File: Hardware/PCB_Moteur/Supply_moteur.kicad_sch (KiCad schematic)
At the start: 32 parts, among them J1 XT30PW-F, J19 XT30PW-F, U2 L6981N33DR

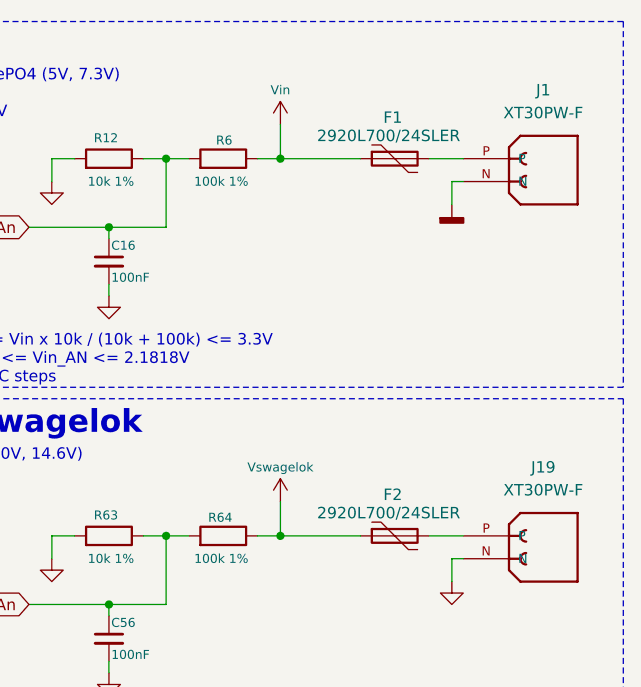
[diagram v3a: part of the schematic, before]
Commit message: fix : add polyfuses and fix 90 deg servo connectors
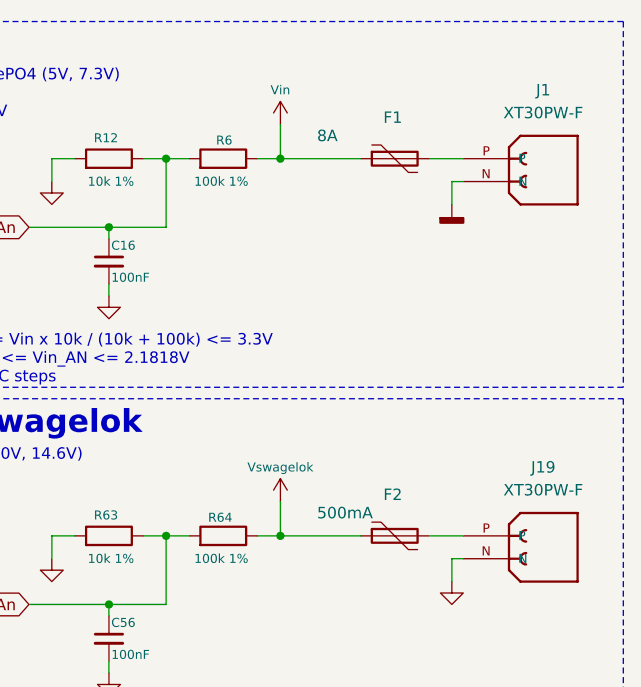
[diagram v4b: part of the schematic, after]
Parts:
- F1: value 2920L700/24SLER -> 8A; DigiKey_Part_Number (none) -> F8136CT-ND; Manufacturer_Part_Number (none) -> 2920L400/15MR
- F2: value 2920L700/24SLER -> 500mA; footprint Fuse:Fuse_2920_7451Metric -> Fuse:Fuse_0805_2012Metric; DigiKey_Part_Number (none) -> 18-0805L020/24YRCT-ND; Manufacturer_Part_Number (none) -> 0805L020/24YR
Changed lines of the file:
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@@
 			)
 		)
-		(property "Value" "2920L700/24SLER"
+		(property "Value" "8A"
 			(at 250.444 25.4 90)
 			(effects
@@
 			)
 		)
-		(property "Datasheet" ""
+		(property "Datasheet" "https://www.digikey.ca/en/products/detail/littelfuse-inc/2920L400-15MR/6234817"
 			(at 259.08 27.94 0)
 			(effects
@@
 		(property "Description" "Resettable fuse"
 			(at 259.08 27.94 0)
+			(effects
+				(font
+					(size 1.27 1.27)
+				)
+				(hide yes)
+			)
+		)
+		(property "DigiKey_Part_Number" "F8136CT-ND"
+			(at 259.08 27.94 90)
+			(effects
+				(font
+					(size 1.27 1.27)
+				)
+				(hide yes)
+			)
+		)
+		(property "Manufacturer_Part_Number" "2920L400/15MR"
+			(at 259.08 27.94 90)
 			(effects
 				(font
@@
 			)
 		)
-		(property "Value" "2920L700/24SLER"
+		(property "Value" "500mA"
 			(at 250.444 67.31 90)
 			(effects
@@
 			)
 		)
-		(property "Footprint" "Fuse:Fuse_2920_7451Metric"
+		(property "Footprint" "Fuse:Fuse_0805_2012Metric"
 			(at 264.16 71.12 0)
 			(effects
@@
 			)
 		)
-		(property "Datasheet" ""
+		(property "Datasheet" "https://www.digikey.ca/en/products/detail/littelfuse-inc/0805L020-24YR/21801844"
 			(at 259.08 69.85 0)
 			(effects
@@
 			(effects
 				(font
+					(size 1.27 1.27)
+				)
+				(hide yes)
+			)
+		)
+		(property "DigiKey_Part_Number" "18-0805L020/24YRCT-ND"
+			(at 259.08 69.85 90)
+			(effects
+				(font
+					(size 1.27 1.27)
+				)
+				(hide yes)
+			)
+		)
+		(property "Manufacturer_Part_Number" "0805L020/24YR"
+			(at 259.08 69.85 90)
+			(effects
+				(font

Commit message: fix : BOM errors, change cutoff freq for moteur, minor fixes for GSE
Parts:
- C6: DigiKey_Part_Number 399-C0603C105K4RACTUCT-ND -> 1276-1029-1-ND; Manufacturer_Part_Number C0603C105K4RACTU -> CL21B105KBFNNNE
- R2, R3: DigiKey_Part_Number P1.5KDBCT-ND -> 311-1.50KCRCT-ND; Manufacturer_Part_Number ERA-3AEB152V -> RC0805FR-071K5L
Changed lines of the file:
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@@
 			)
 		)
-		(property "Datasheet" "https://www.digikey.ca/en/products/detail/kemet/C0603C105K4RACTU/2199788"
+		(property "Datasheet" "https://www.digikey.ca/en/products/detail/samsung-electro-mechanics/CL21B105KBFNNNE/3886687"
 			(at 93.98 71.12 0)
 			(effects
@@
 			)
 		)
-		(property "DigiKey_Part_Number" "399-C0603C105K4RACTUCT-ND"
+		(property "DigiKey_Part_Number" "1276-1029-1-ND"
 			(at 93.98 71.12 90)
 			(effects
@@
 			)
 		)
-		(property "Manufacturer_Part_Number" "C0603C105K4RACTU"
+		(property "Manufacturer_Part_Number" "CL21B105KBFNNNE"
 			(at 93.98 71.12 90)
 			(effects
@@
 			)
 		)
-		(property "Datasheet" "https://www.digikey.ca/en/products/detail/panasonic-electronic-components/ERA-3AEB152V/1465858"
+		(property "Datasheet" "https://www.digikey.ca/en/products/detail/yageo/RC0805FR-071K5L/727496"
 			(at 114.3 111.76 0)
 			(effects
@@
 			)
 		)
-		(property "DigiKey_Part_Number" "P1.5KDBCT-ND"
+		(property "DigiKey_Part_Number" "311-1.50KCRCT-ND"
 			(at 114.3 111.76 90)
 			(effects
@@
 			)
 		)
-		(property "Manufacturer_Part_Number" "ERA-3AEB152V"
+		(property "Manufacturer_Part_Number" "RC0805FR-071K5L"
 			(at 114.3 111.76 90)
 			(effects
@@
 			)
 		)
-		(property "Datasheet" "https://www.digikey.ca/en/products/detail/panasonic-electronic-components/ERA-3AEB152V/1465858"
+		(property "Datasheet" "https://www.digikey.ca/en/products/detail/yageo/RC0805FR-071K5L/727496"
 			(at 114.3 105.41 0)
 			(effects
@@
 			)
 		)
-		(property "DigiKey_Part_Number" "P1.5KDBCT-ND"
+		(property "DigiKey_Part_Number" "311-1.50KCRCT-ND"
 			(at 114.3 105.41 90)
 			(effects
@@
 			)
 		)
-		(property "Manufacturer_Part_Number" "ERA-3AEB152V"
+		(property "Manufacturer_Part_Number" "RC0805FR-071K5L"
 			(at 114.3 105.41 90)
 			(effects

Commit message: feature : Done v1 and send to fab
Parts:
- removed NT0: NetTie_2, NetTie:NetTie-4_SMD_Pad0.5mm, symbol Device:NetTie_2
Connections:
- net GND is gone; now on net AGND3V3: C14.2, C15.2, C16.2, C17.2, C56.2, C7.2, C8.2, C9.2, D2.1 (K), J19.N, R11.1, R12.2, R63.2
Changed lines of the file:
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@@
 	(wire
 		(pts
-			(xy 115.57 115.57) (xy 115.57 116.84)
+			(xy 115.57 118.11) (xy 115.57 119.38)
 		)
 		(stroke
@@
 	(wire
 		(pts
-			(xy 114.3 115.57) (xy 115.57 115.57)
-		)
-		(stroke
-			(width 0)
-			(type default)
-		)
-	)
-	(wire
-		(pts
 			(xy 107.95 109.22) (xy 110.49 109.22)
 		)
@@
 	(wire
 		(pts
-			(xy 107.95 115.57) (xy 107.95 116.84)
+			(xy 107.95 118.11) (xy 107.95 119.38)
 		)
 		(stroke
@@
 	(wire
 		(pts
-			(xy 109.22 115.57) (xy 107.95 115.57)
+			(xy 107.95 118.11) (xy 115.57 118.11)
 		)
 		(stroke
@@
 				)
 				(justify right)
+				(hide yes)
+			)
+		)
+	)
+	(global_label "GND"
+		(shape input)
+		(at 115.57 118.11 0)
+		(fields_autoplaced yes)
+		(effects
+			(font
+				(size 1.27 1.27)
+			)
+			(justify left)
+		)
+		(property "Intersheetrefs" "${INTERSHEET_REFS}"
+			(at 122.4257 118.11 0)
+			(effects
+				(font
+					(size 1.27 1.27)
+				)
+				(justify left)
 				(hide yes)
 			)
@@
 	)
 	(symbol
-		(lib_id "Device:NetTie_2")
-		(at 111.76 115.57 0)
-		(unit 1)
-		(exclude_from_sim no)
-		(in_bom no)
-		(on_board yes)
-		(dnp no)
-		(fields_autoplaced yes)
-		(property "Reference" "NT0"
-			(at 111.76 110.49 0)
-			(effects
-				(font
-					(size 1.27 1.27)
-				)
-				(hide yes)
-			)
-		)
-		(property "Value" "NetTie_2"
-			(at 111.76 113.03 0)
-			(effects
-				(font
-					(size 1.27 1.27)
-				)
-				(hide yes)
-			)
-		)
-		(property "Footprint" "NetTie:NetTie-4_SMD_Pad0.5mm"
-			(at 111.76 115.57 0)
-			(effects
-				(font
-					(size 1.27 1.27)
-				)
-				(hide yes)
-			)
-		)
-		(property "Datasheet" "-"
-			(at 111.76 115.57 0)
-			(effects
-				(font
-					(size 1.27 1.27)
-				)
-				(hide yes)
-			)
-		)
-		(property "Description" "Net tie, 2 pins"
-			(at 111.76 115.57 0)
-			(effects
-				(font
-					(size 1.27 1.27)
-				)
-				(hide yes)
-			)
-		)
-		(property "DigiKey_Part_Number" "-"
-			(at 111.76 115.57 0)
-			(effects
-				(font
-					(size 1.27 1.27)
-				)
-				(hide yes)
-			)
-		)
-		(property "Manufacturer_Part_Number" "-"
-			(at 111.76 115.57 0)
-			(effects
-				(font
-					(size 1.27 1.27)
-				)
-				(hide yes)
-			)
-		)
-		(pin "2"
-		)
-		(pin "1"
-		)
-		(instances
-			(project "PCB_moteur"
-				(path "/b0d87684-7b1c-41d8-8358-755aa327573e/92d1df5d-a307-4eea-a65c-ade4cb0ad548"
-					(reference "NT0")
-					(unit 1)
-				)
-			)
-		)
-	)
-	(symbol
 		(lib_id "Device:C_Small")
 		(at 49.53 114.3 0)
@@
 	(symbol
 		(lib_id "power:GND")
-		(at 115.57 116.84 0)
+		(at 115.57 119.38 0)
 		(unit 1)
 		(exclude_from_sim no)
@@
 		(fields_autoplaced yes)
 		(property "Reference" "#PWR0109"
-			(at 115.57 123.19 0)
+			(at 115.57 125.73 0)
 			(effects
 				(font
@@
 		)
 		(property "Value" "GND"
-			(at 115.57 121.92 0)
+			(at 115.57 124.46 0)
 			(effects
 				(font
@@
 		)
 		(property "Footprint" ""
-			(at 115.57 116.84 0)
+			(at 115.57 119.38 0)
 			(effects
 				(font
@@
 		)
 		(property "Datasheet" ""
-			(at 115.57 116.84 0)
+			(at 115.57 119.38 0)
 			(effects
 				(font
@@
 		)
 		(property "Description" ""
-			(at 115.57 116.84 0)
+			(at 115.57 119.38 0)
 			(effects
 				(font
@@
 	(symbol
 		(lib_id "power:GNDD")
-		(at 107.95 116.84 0)
+		(at 107.95 119.38 0)
 		(unit 1)
 		(exclude_from_sim no)
@@
 		(fields_autoplaced yes)
 		(property "Reference" "#PWR0107"
+			(at 107.95 125.73 0)
+			(effects
+				(font
+					(size 1.27 1.27)
+				)
+				(hide yes)
+			)
+		)
+		(property "Value" "AGND3V3"
 			(at 107.95 123.19 0)
 			(effects
@@
 			)
 		)
-		(property "Value" "AGND3V3"
-			(at 107.95 120.65 0)
-			(effects
-				(font
-					(size 1.27 1.27)
-				)
-				(hide yes)
-			)
-		)
 		(property "Footprint" ""
-			(at 107.95 116.84 0)
+			(at 107.95 119.38 0)
 			(effects
 				(font
@@
 		)
 		(property "Datasheet" ""
-			(at 107.95 116.84 0)
+			(at 107.95 119.38 0)
 			(effects
 				(font
@@
 		)
 		(property "Description" "Power symbol creates a global label with name \"GNDD\" , digital ground"
-			(at 107.95 116.84 0)
-			(effects
-				(font
+			(at 107.95 119.38 0)
+			(effects
+				(font
